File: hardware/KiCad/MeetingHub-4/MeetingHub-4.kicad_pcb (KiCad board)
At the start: 4 copper layers, 160.1 x 134 mm, 75 parts, among them J1 USB-C POWER IN, J2 TRRS Notebook 1, J3 TRRS Notebook 2, J4 TRRS Notebook 3, J5 TRRS Notebook 4, J6 Headset (User), K1 Select NB1, K2 Select NB2, K3 Select NB3, K4 Select NB4, SW1 MUTE, SW2 Select NB1, SW3 Select NB2, SW4 Select NB3, SW5 Select NB4, U1 NE5532, U2 NJM4556A

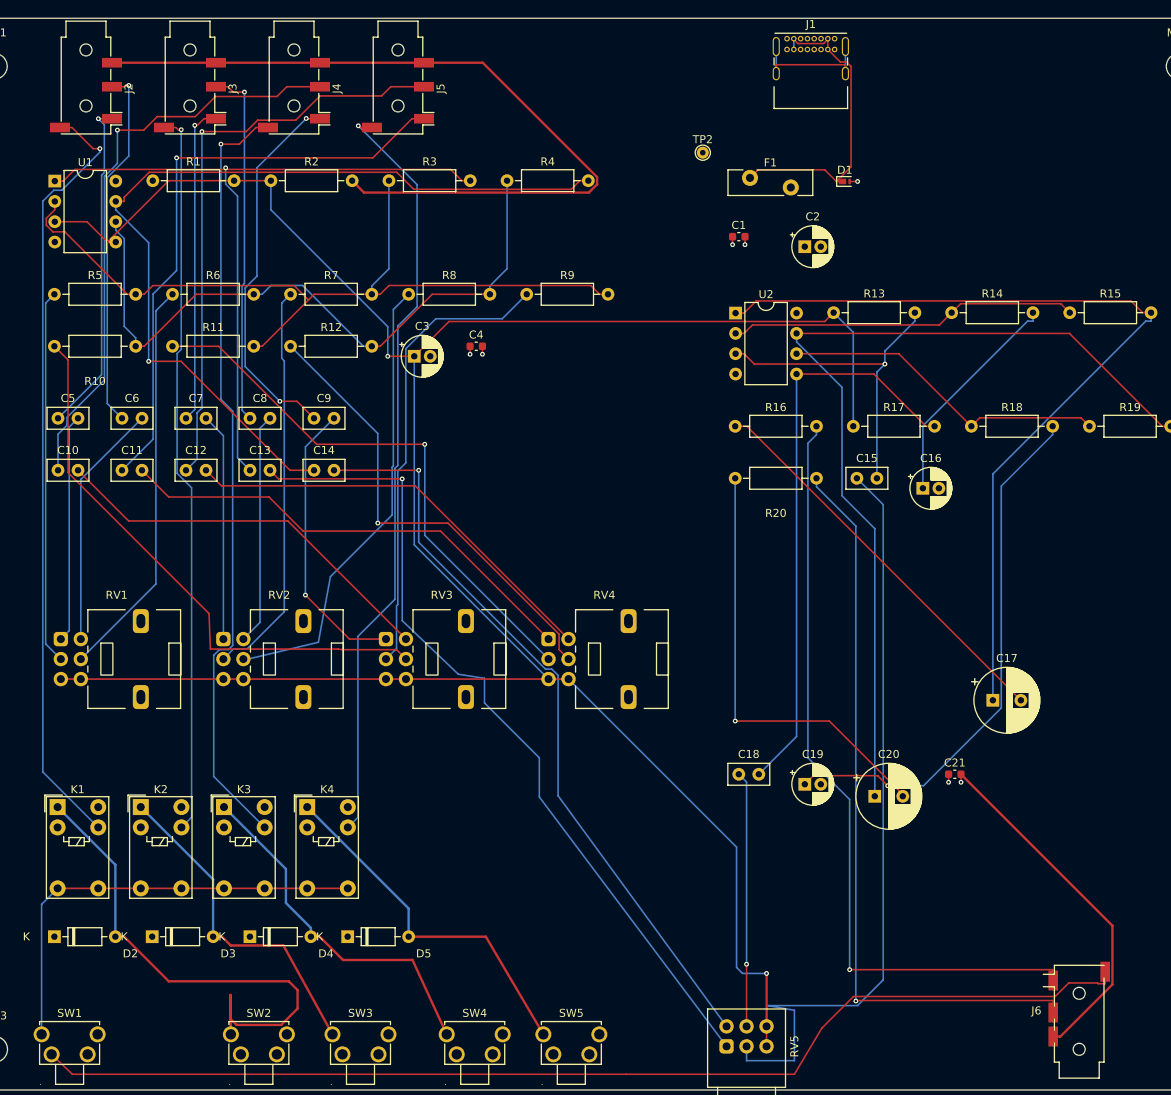
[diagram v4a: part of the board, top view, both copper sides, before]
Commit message: Fix J2-J6 pad mismatch and J1 orientation flagged by JLCPCB DFM
SMT026081260178_Y11: J2-J6 SMD pads resized to match real PJ-320D
datasheet (1.5x3.0mm), local traces rerouted for clearance. J1
rotated 180 deg to face outward (was mounted backwards). Gerbers v13.0.
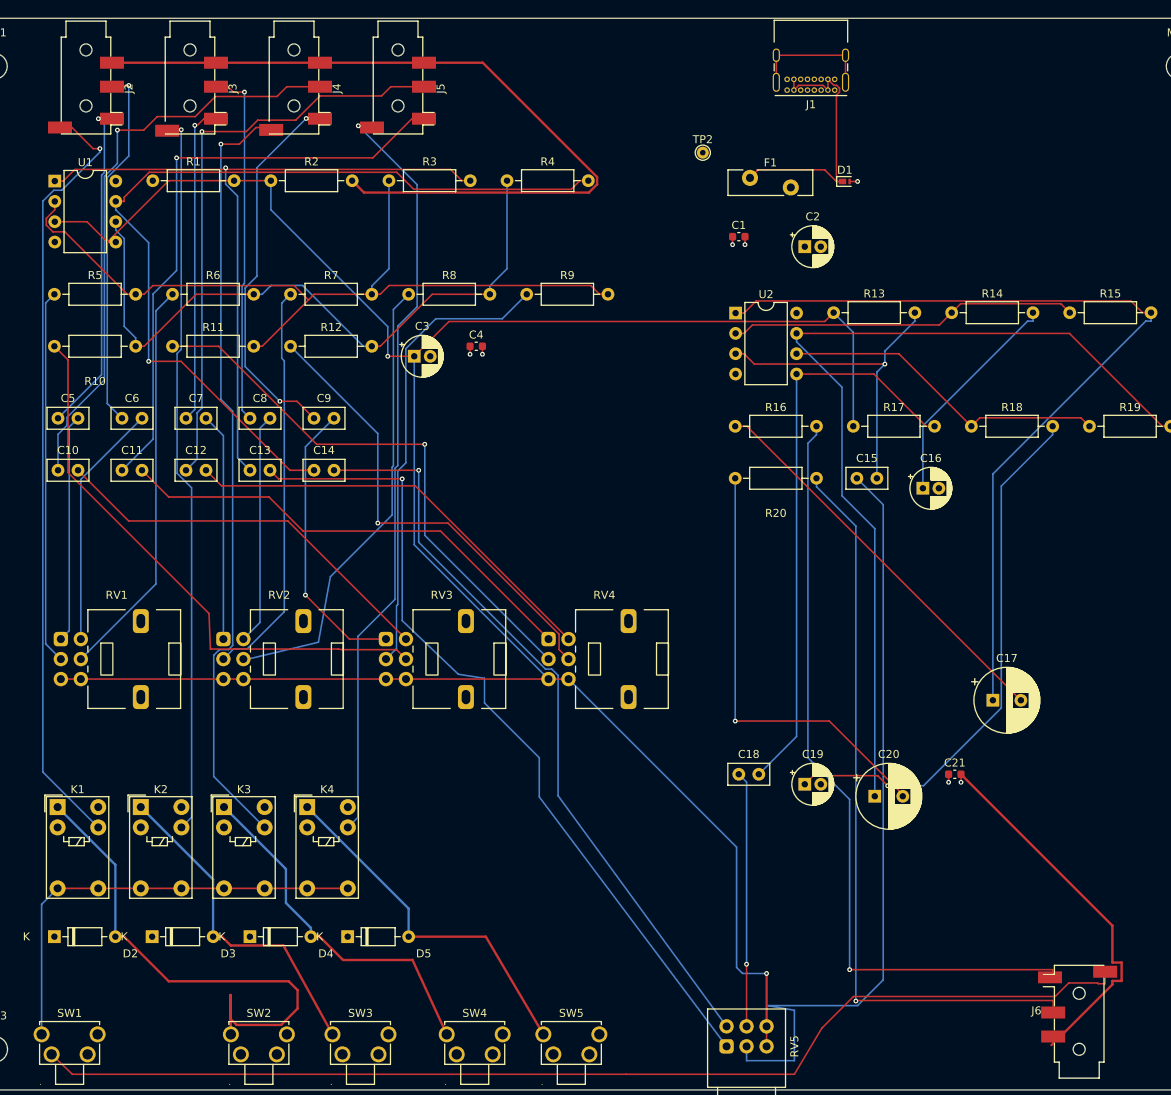
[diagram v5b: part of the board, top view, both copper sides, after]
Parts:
- moved J1 8.77 mm to (171.0, 94.0), turned to 180 degrees
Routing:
- net Net-(D1-K): track 39.1 -> 33.8 mm
- net GND: track 148.5 -> 150.8 mm
- net unconnected-(J1-SHIELD-PadS1): track 17.6 -> 15.4 mm

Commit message: Rascunho projeto após fabricação com prblemas
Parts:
- removed SW1: MUTE, MeetingHub-4:SW_SHOUHAN_TS665ZJ
- C1, C21, C4: footprint C_0603_1608Metric -> Capacitor_SMD:C_0603_1608Metric
- D1: footprint Nexperia_DSN1608-2_1.6x0.8mm -> Diode_SMD:Nexperia_DSN1608-2_1.6x0.8mm
- RV5: value Potentiometer_Alps_RK097_Dual_Horizontal -> 10k Master
- SW2: value Select NB1 -> Select NB1 (latching); footprint MeetingHub-4:SW_SHOUHAN_TS665ZJ -> MeetingHub-4:SW_PushLock_PS-22F03
- SW3: value Select NB2 -> Select NB2 (latching); footprint MeetingHub-4:SW_SHOUHAN_TS665ZJ -> MeetingHub-4:SW_PushLock_PS-22F03
- SW4: value Select NB3 -> Select NB3 (latching); footprint MeetingHub-4:SW_SHOUHAN_TS665ZJ -> MeetingHub-4:SW_PushLock_PS-22F03
- SW5: value Select NB4 -> Select NB4 (latching); footprint MeetingHub-4:SW_SHOUHAN_TS665ZJ -> MeetingHub-4:SW_PushLock_PS-22F03
- moved SW2 11.1 mm to (88.0, 213.0), turned to 180 degrees
- moved SW5 6.88 mm to (145.0, 213.0), turned to 180 degrees
- moved SW3 4.77 mm to (107.0, 213.0), turned to 180 degrees
- moved SW4 0.26 mm to (126.0, 213.0), turned to 180 degrees
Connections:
- D2 pad 1: GND -> Net-(D2-K)
- D2 pad 2: Net-(D2-A) -> GND
- D3 pad 1: GND -> Net-(D3-K)
- D3 pad 2: Net-(D3-A) -> GND
- D4 pad 1: GND -> Net-(D4-K)
- D4 pad 2: Net-(D4-A) -> GND
- D5 pad 1: GND -> Net-(D5-K)
- D5 pad 2: Net-(D5-A) -> GND
- K1 pad 1: Net-(D2-A) -> unconnected-(K1-Pad1)
- K1 pad 10: unconnected-(K1-Pad10) -> NB1_MIC
- K1 pad 5: Net-(SW1-B) -> HEADSET_MIC
- K1 pad 6: Net-(SW1-B) -> HEADSET_MIC
- K1 pad 9: NB1_MIC -> Net-(D2-K)
- K2 pad 1: Net-(D3-A) -> unconnected-(K2-Pad1)
- K2 pad 10: unconnected-(K2-Pad10) -> NB2_MIC
- K2 pad 5: Net-(SW1-B) -> HEADSET_MIC
- K2 pad 6: Net-(SW1-B) -> HEADSET_MIC
- K2 pad 9: NB2_MIC -> Net-(D3-K)
- K3 pad 1: Net-(D4-A) -> unconnected-(K3-Pad1)
- K3 pad 10: unconnected-(K3-Pad10) -> NB3_MIC
- K3 pad 5: Net-(SW1-B) -> HEADSET_MIC
- K3 pad 6: Net-(SW1-B) -> HEADSET_MIC
- K3 pad 9: NB3_MIC -> Net-(D4-K)
- K4 pad 1: Net-(D5-A) -> unconnected-(K4-Pad1)
- K4 pad 10: unconnected-(K4-Pad10) -> NB4_MIC
- K4 pad 5: Net-(SW1-B) -> HEADSET_MIC
- K4 pad 6: Net-(SW1-B) -> HEADSET_MIC
- K4 pad 9: NB4_MIC -> Net-(D5-K)
- RV1 pad 1: Net-(C5-Pad2) -> VBIAS
- RV1 pad 3: VBIAS -> Net-(C5-Pad2)
- RV1 pad 4: Net-(C6-Pad2) -> VBIAS
- RV1 pad 6: VBIAS -> Net-(C6-Pad2)
- RV2 pad 1: Net-(C7-Pad2) -> VBIAS
- RV2 pad 3: VBIAS -> Net-(C7-Pad2)
- RV2 pad 4: Net-(C8-Pad2) -> VBIAS
- RV2 pad 6: VBIAS -> Net-(C8-Pad2)
- RV3 pad 1: Net-(C9-Pad2) -> VBIAS
- RV3 pad 3: VBIAS -> Net-(C9-Pad2)
- RV3 pad 4: Net-(C10-Pad2) -> VBIAS
- RV3 pad 6: VBIAS -> Net-(C10-Pad2)
- RV4 pad 1: Net-(C11-Pad2) -> VBIAS
- RV4 pad 3: VBIAS -> Net-(C11-Pad2)
- RV4 pad 4: Net-(C12-Pad2) -> VBIAS
- RV4 pad 6: VBIAS -> Net-(C12-Pad2)
- RV5 pad 1: Net-(C13-Pad2) -> VBIAS
- RV5 pad 3: VBIAS -> Net-(C13-Pad2)
- RV5 pad 4: Net-(C14-Pad2) -> VBIAS
- RV5 pad 6: VBIAS -> Net-(C14-Pad2)
- SW2 pad 2: Net-(D2-A) -> Net-(D2-K)
- SW3 pad 2: Net-(D3-A) -> Net-(D3-K)
- SW4 pad 2: Net-(D4-A) -> Net-(D4-K)
- SW5 pad 2: Net-(D5-A) -> Net-(D5-K)
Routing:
- net VBIAS: track 308.8 -> 176.2 mm
- net Net-(D2-A): track 64.5 -> 0.00 mm
- net HEADSET_MIC: track 139.9 -> 198.0 mm, vias 0 -> 1
- net Net-(SW1-B): track 55.4 -> 0.00 mm
- net Net-(D5-A): track 45.3 -> 0.00 mm
- net Net-(D4-A): track 44.8 -> 0.00 mm
- net Net-(D3-A): track 41.9 -> 0.00 mm
- net Net-(C13-Pad2): track 104.4 -> 65.4 mm
- net Net-(C14-Pad2): track 94.6 -> 58.9 mm
- net Net-(C12-Pad2): track 54.1 -> 27.0 mm
- net Net-(C7-Pad2): track 28.5 -> 3.08 mm
- net Net-(C10-Pad2): track 49.7 -> 28.9 mm
- net Net-(C6-Pad2): track 30.8 -> 10.8 mm
- net Net-(C11-Pad2): track 59.6 -> 40.5 mm
- net NB1_MIC: track 97.3 -> 87.5 mm
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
